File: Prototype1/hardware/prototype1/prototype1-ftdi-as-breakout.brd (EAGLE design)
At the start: 81 x 40 mm, 31 parts, among them IC2 LDL112D33R, IC5 M95010-WMN6P, J7 TMP BATTERY, U2 ESP-WROOM-32

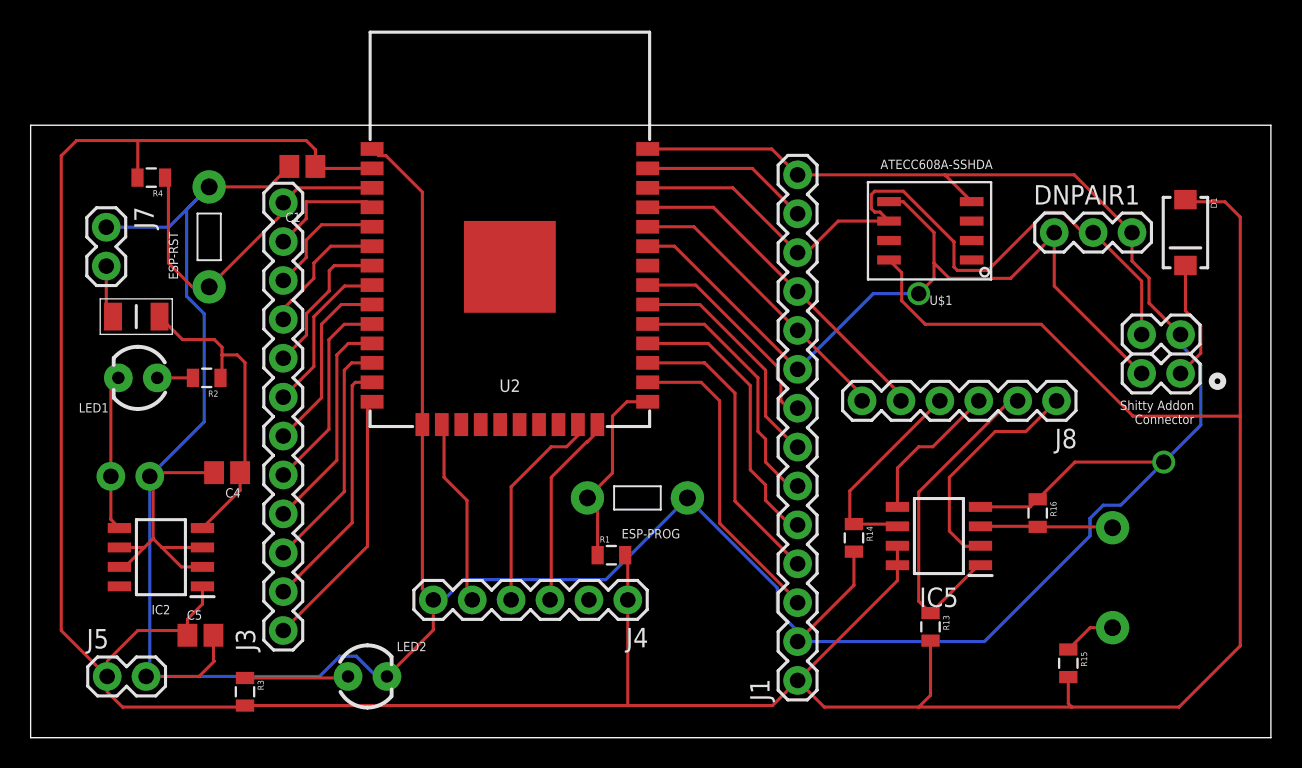
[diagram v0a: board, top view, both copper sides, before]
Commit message: added logo and fixed drc error
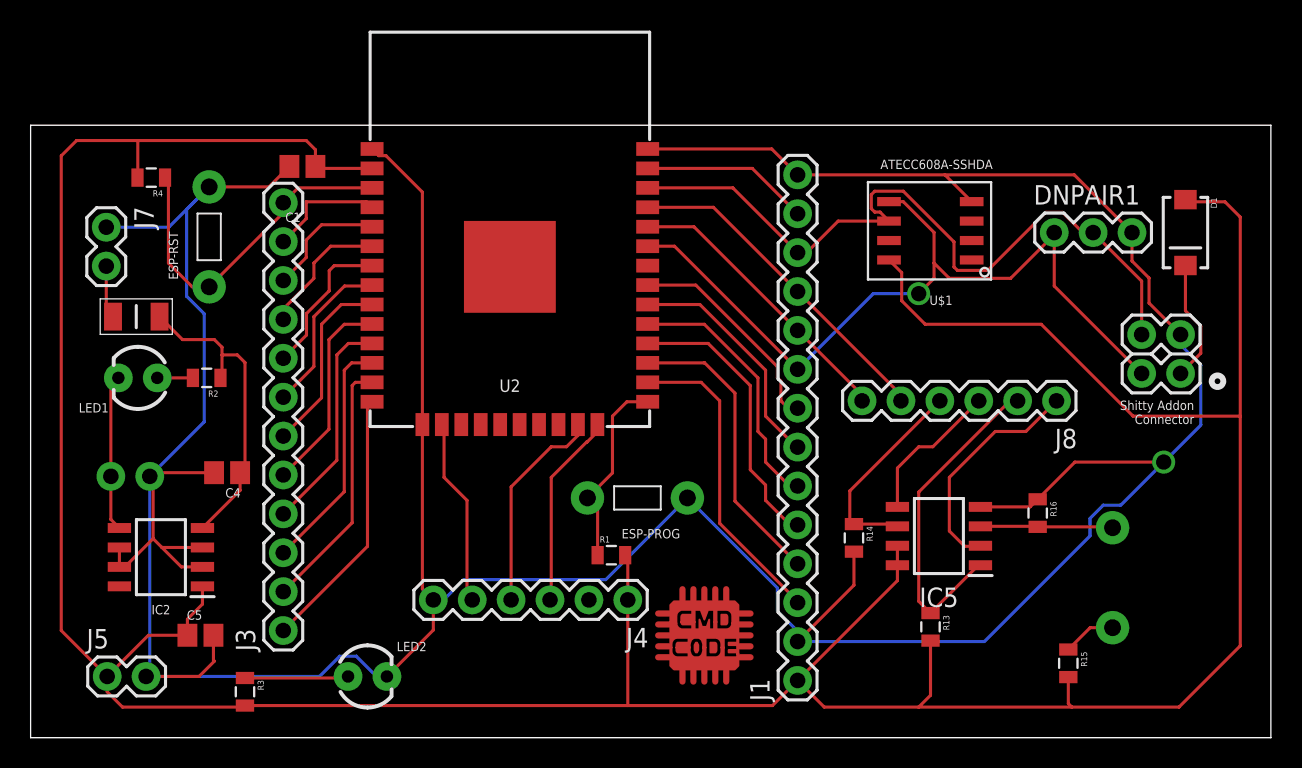
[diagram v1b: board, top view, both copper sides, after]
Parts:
- added U$2: CMD_C0DE_LOGOCMD_CODE_LOGO_TOP_COPPER, logos:CMD_C0DE_LOGO_TOP_COPPER
